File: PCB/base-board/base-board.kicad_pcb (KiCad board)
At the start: 2 copper layers, 70 x 90 mm, 24 parts, among them J1 POWER, J2 ENCODER1, J3 ENCODER2, J4 SENSOR, J5 MOTOR1, J6 MOTOR2, SW1 SW1, SW2 SW2, SW3 RESET, U1 AE-TC78H653FTG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

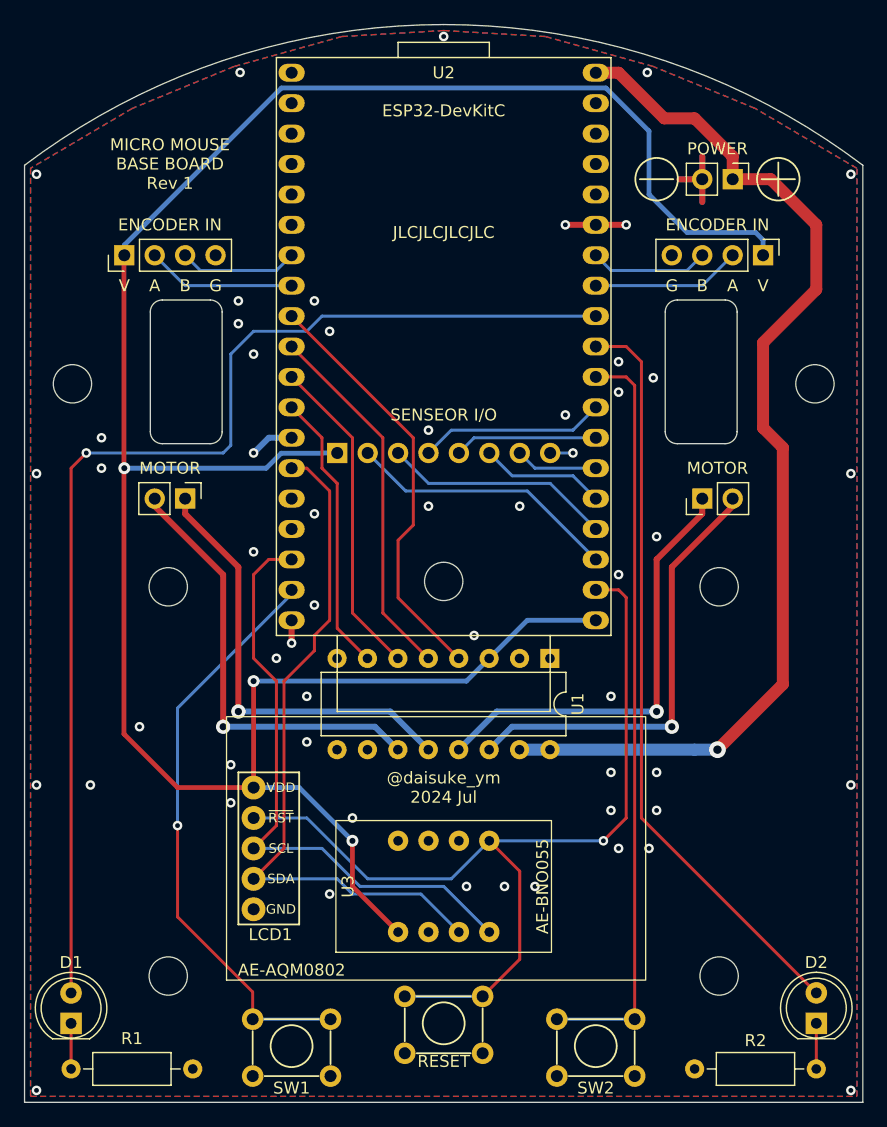
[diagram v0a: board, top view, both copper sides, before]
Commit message: 設計ミス発覚 液晶のマウント位置がギヤードモーターとかぶっていた 修正した
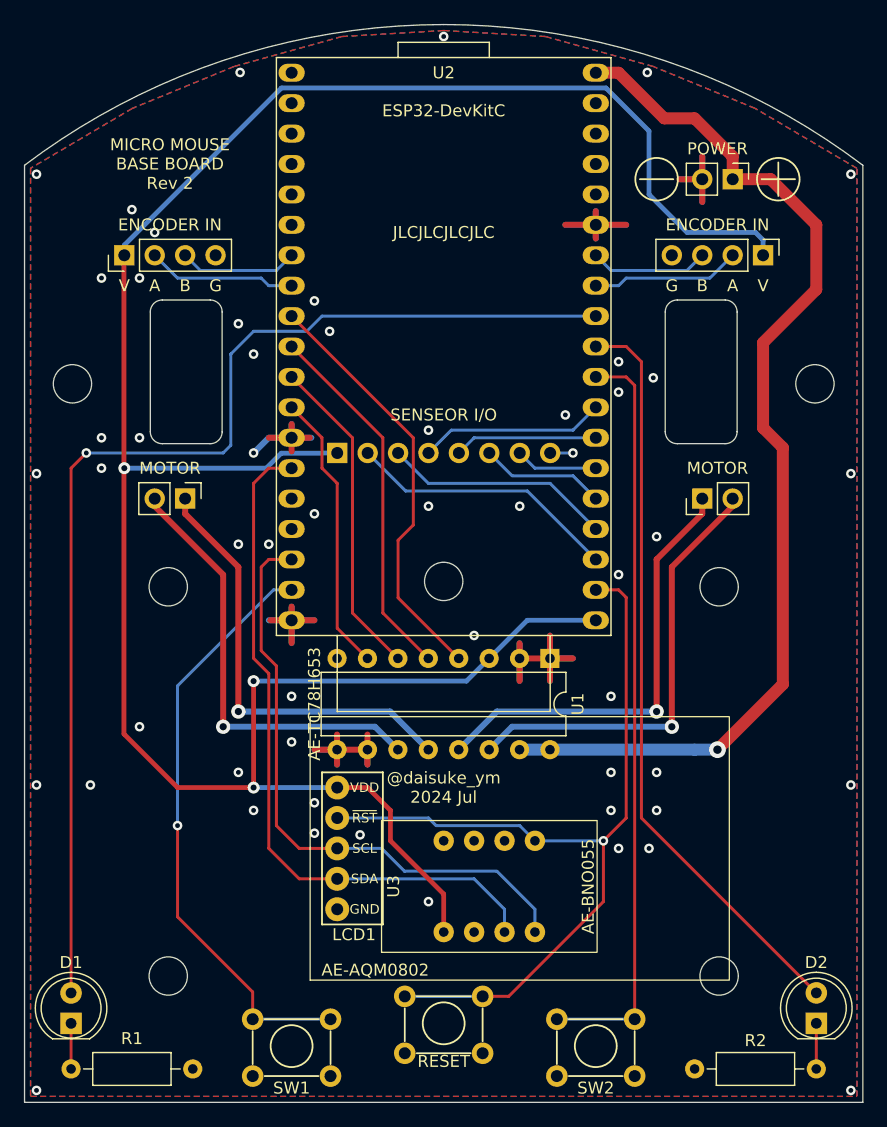
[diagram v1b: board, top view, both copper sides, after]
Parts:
- moved LCD1 6.99 mm to (141.1, 110.8)
- moved U3 3.81 mm to (153.8, 114.0)
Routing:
- net GND: track 24.0 -> 87.9 mm, vias 55 -> 54
- net /RESET: track 78.4 -> 71.9 mm
- net +3.3V: track 199.1 -> 204.0 mm
- net /SW1: track 48.9 -> 49.8 mm
- net /SCL: track 50.7 -> 51.3 mm
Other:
- board text added: "AE-TC78H653"
- board text added: "MICRO MOUSE BASE BOARD Rev 2"
- board text removed: "MICRO MOUSE BASE BOARD Rev 1"
